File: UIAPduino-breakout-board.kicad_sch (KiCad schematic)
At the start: 13 parts, among them J1 Conn_01x20_Pin, J2 Conn_01x20_Socket, J3 Barrel_Jack_Switch, U3 L7805

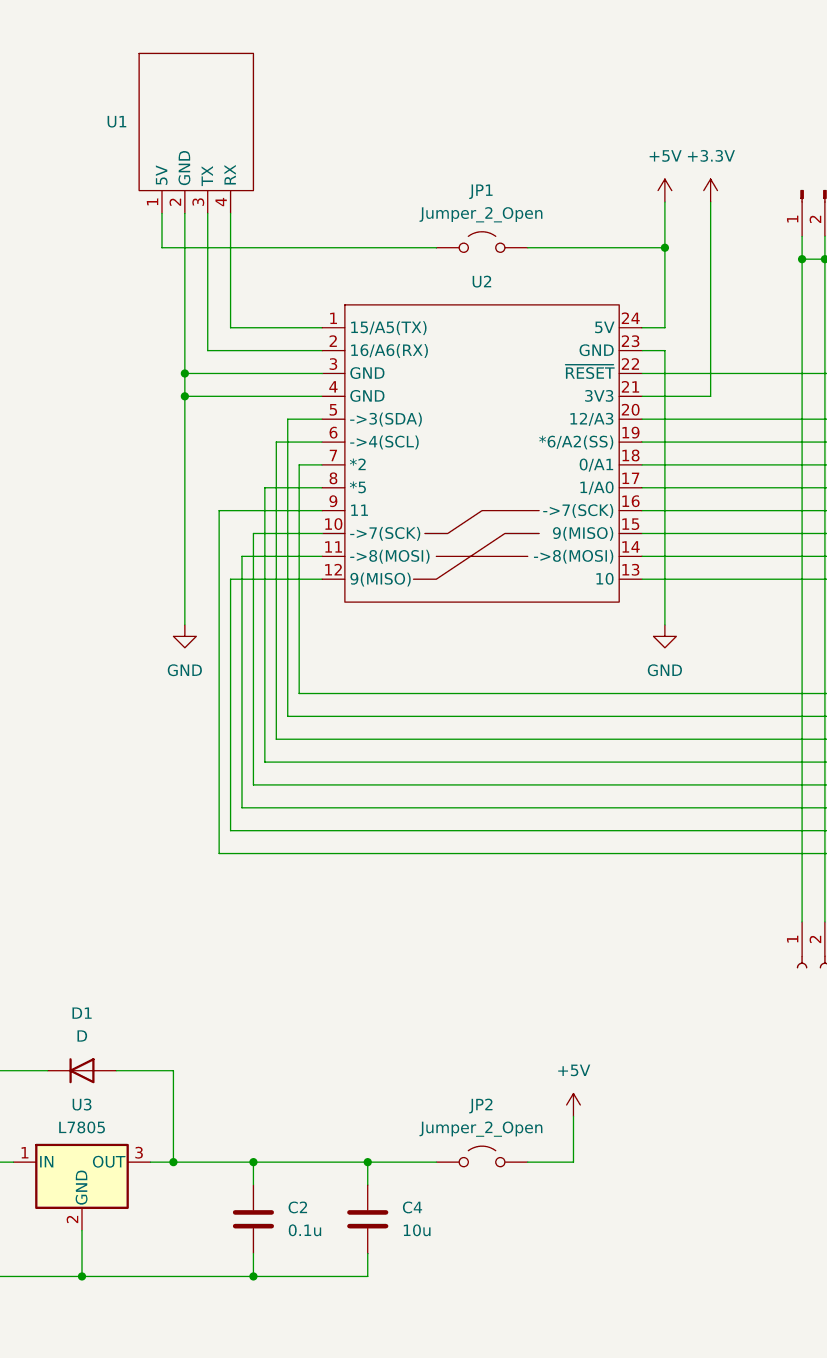
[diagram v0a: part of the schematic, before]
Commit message: ジャンパをスイッチに変更
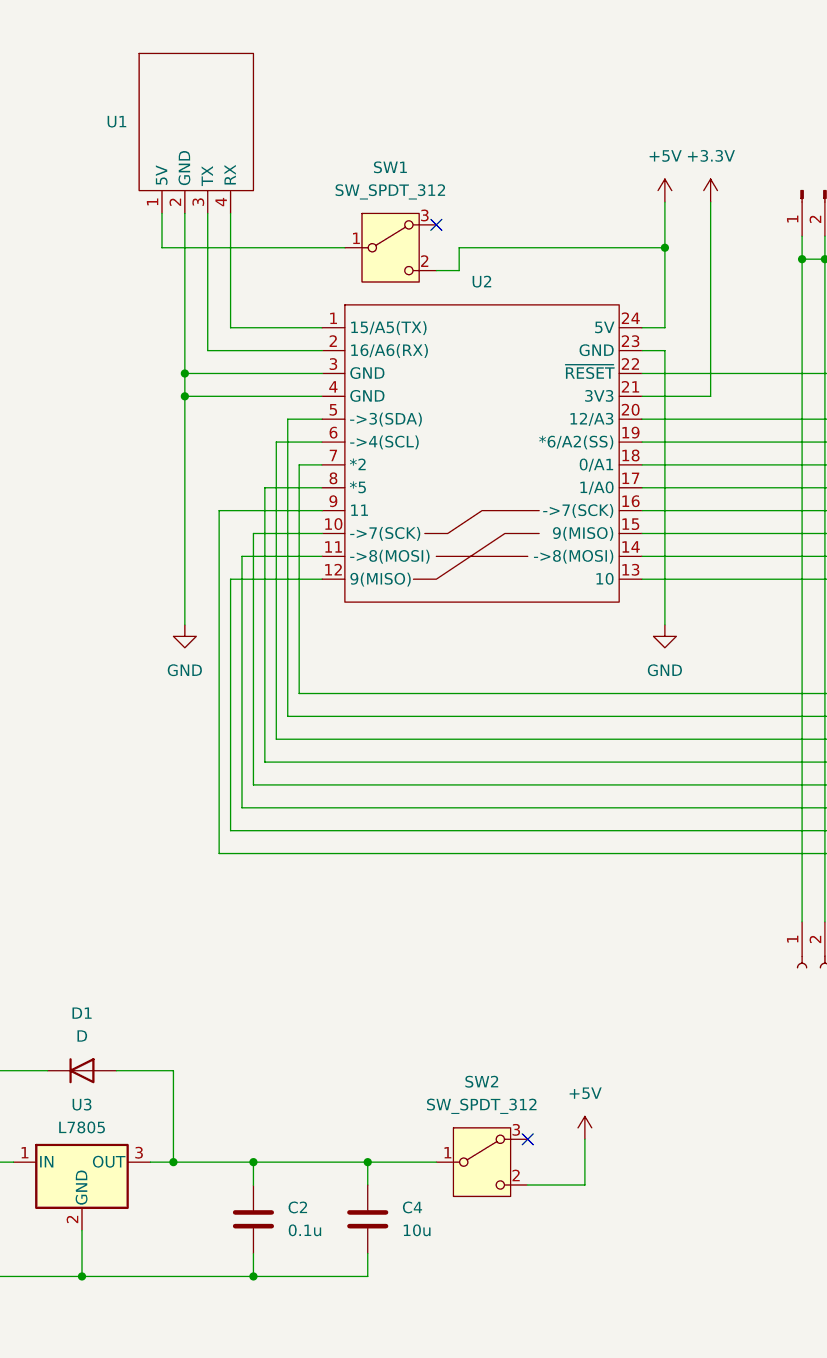
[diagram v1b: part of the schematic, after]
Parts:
- removed JP1, JP2: Jumper_2_Open, Jumper:SolderJumper-2_P1.3mm_Open_TrianglePad1.0x1.5mm, symbol Jumper:Jumper_2_Open
- added SW1, SW2: SW_SPDT_312, Button_Switch_THT:SW_Slide-03_Wuerth-WS-SLTV_10x2.5x6.4_P2.54mm, symbol Switch:SW_SPDT_312
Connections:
- net +5V: now also SW1.2 (C), SW2.2 (C)
- net at U1.1 (5V): now also SW1.1 (B)
- net at C2.1, C4.1, D1.2 (A)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: now also SW2.1 (B)
- no-connect marks 0 -> 2

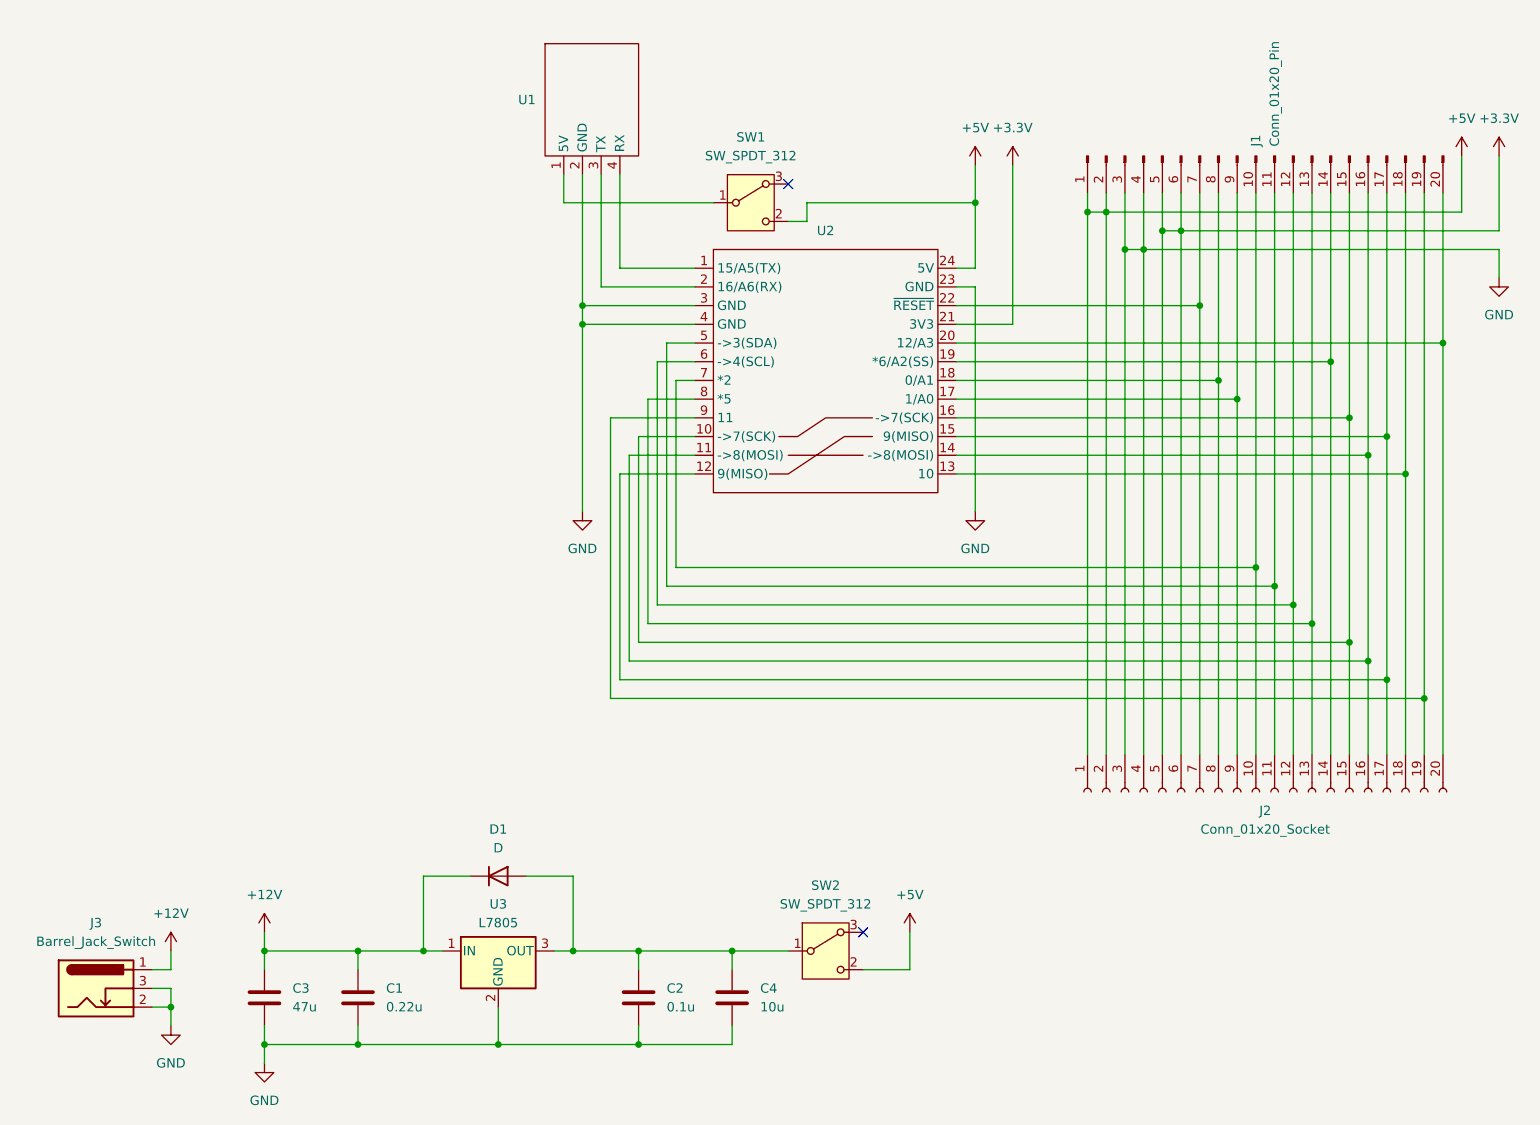
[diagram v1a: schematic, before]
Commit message: UART 接続先切り替え用スイッチを追加
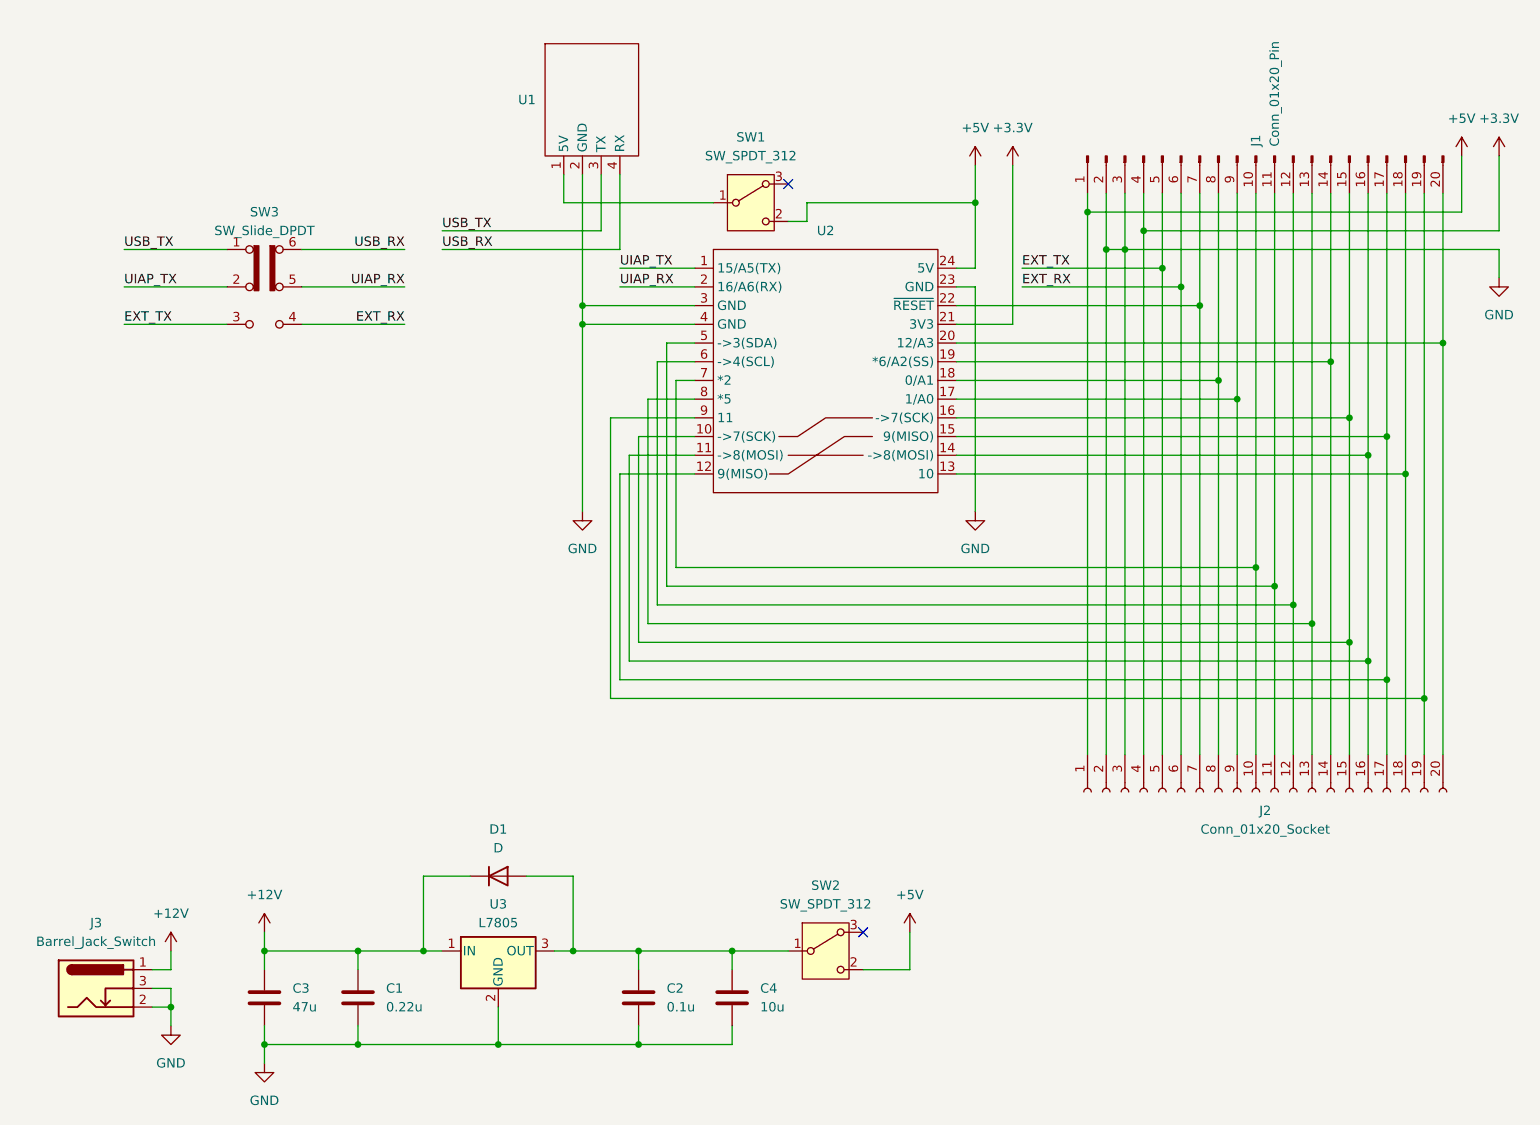
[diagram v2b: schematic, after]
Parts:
- added SW3: SW_Slide_DPDT, Button_Switch_THT:SW_CK_JS202011CQN_DPDT_Straight, symbol Switch:SW_Slide_DPDT
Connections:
- net +3.3V: now also J1.4 (Pin_4), J2.4 (Pin_4); no longer J1.5 (Pin_5), J1.6 (Pin_6), J2.5 (Pin_5), J2.6 (Pin_6)
- net +5V: no longer J1.2 (Pin_2), J2.2 (Pin_2)
- net GND: now also J1.2 (Pin_2), J2.2 (Pin_2); no longer J1.4 (Pin_4), J2.4 (Pin_4)
- net UIAP_RX: now reaches U2.2 (16/A6(RX))
- net UIAP_RX: now also SW3.5 (B); no longer U1.3 (TX)
- net UIAP_TX: now reaches U2.1 (15/A5(TX))
- net UIAP_TX: now also SW3.2 (B); no longer U1.4 (RX)
- new net EXT_RX: J1.6 (Pin_6), J2.6 (Pin_6), SW3.4 (A)
- new net EXT_TX: J1.5 (Pin_5), J2.5 (Pin_5), SW3.3 (C)
- new net USB_RX: SW3.6 (C), U1.4 (RX)
- new net USB_TX: SW3.1 (A), U1.3 (TX)

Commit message: 配線修正
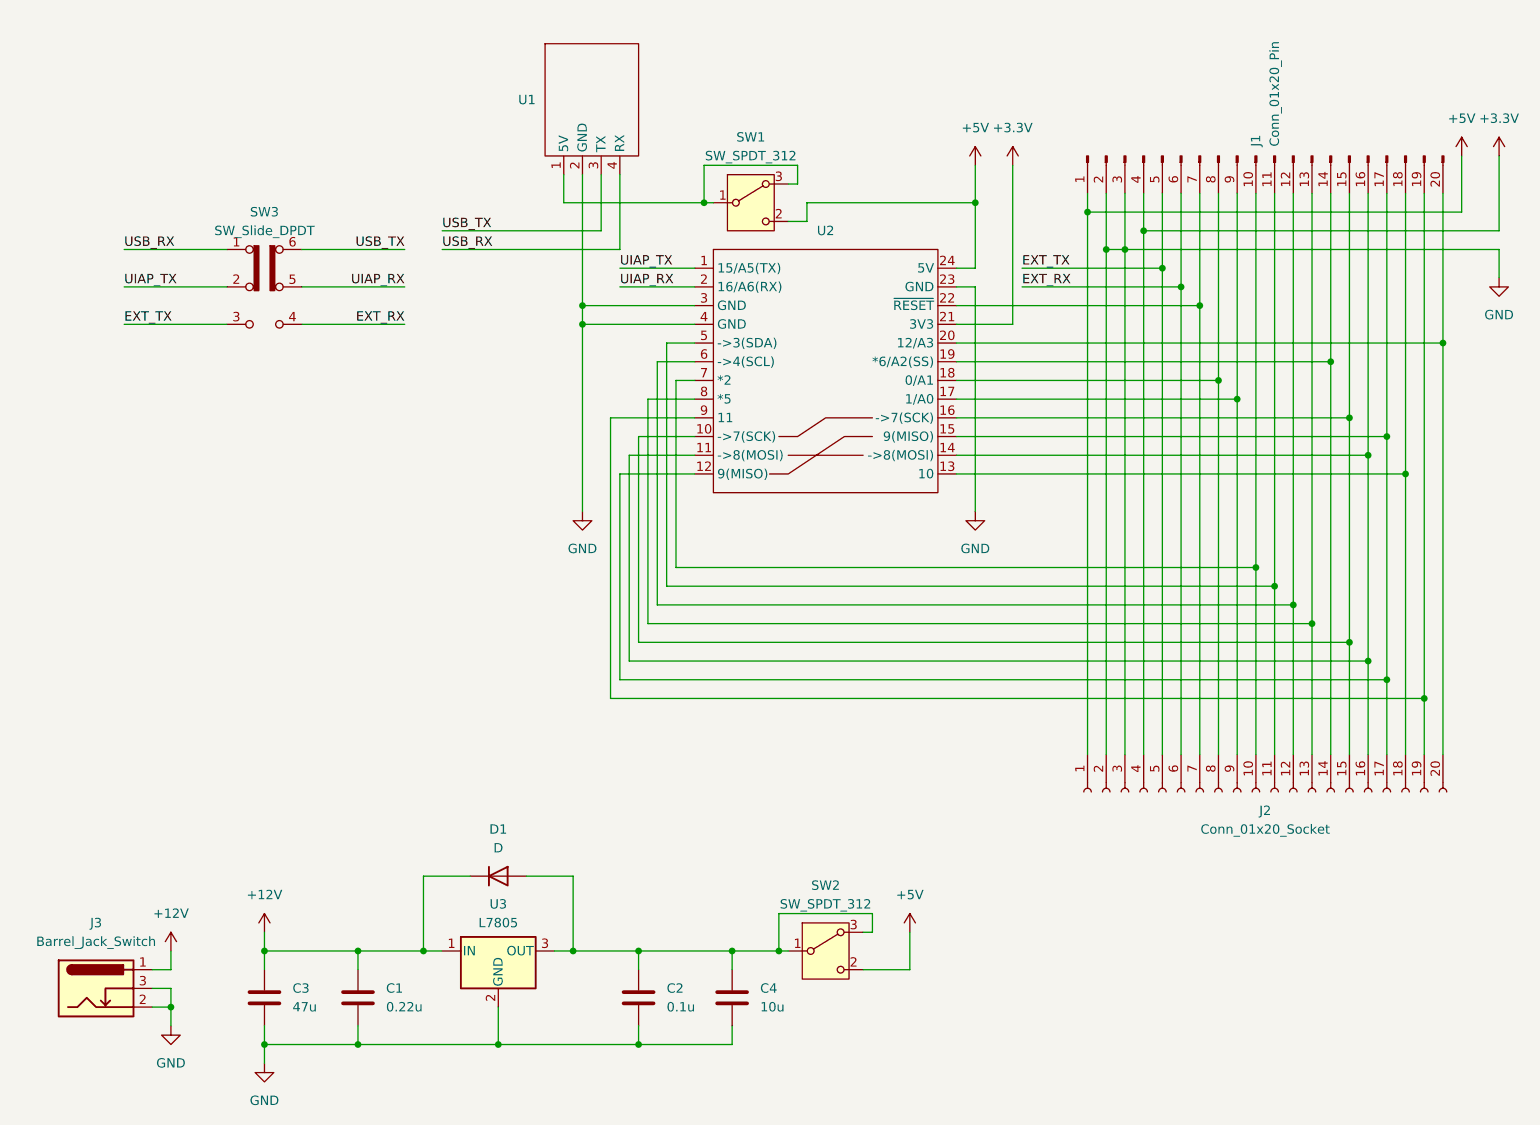
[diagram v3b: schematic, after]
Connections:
- net USB_RX: now also SW3.1 (A); no longer SW3.6 (C)
- net USB_TX: now also SW3.6 (C); no longer SW3.1 (A)
- net at C2.1, C4.1, D1.2 (A)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: now also SW2.3 (A)
- net at SW1.1 (B), U1.1 (5V): now also SW1.3 (A)
- no-connect marks 2 -> 0
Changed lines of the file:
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@@
+	)
+	(junction
+		(at 146.05 153.67)
+		(diameter 0)
+		(color 0 0 0 0)
 	)
 	(junction
@@
 		(color 0 0 0 0)
 	)
-	(no_connect
-		(at 147.32 49.53)
-	)
-	(no_connect
-		(at 157.48 151.13)
+	(junction
+		(at 135.89 52.07)
+		(diameter 0)
+		(color 0 0 0 0)
 	)
 	(wire
@@
 	(wire
 		(pts
+			(xy 158.75 148.59) (xy 146.05 148.59)
+		)
+		(stroke
+			(width 0)
+			(type default)
+		)
+	)
+	(wire
+		(pts
 			(xy 127 166.37) (xy 127 163.83)
 		)
@@
 	(wire
 		(pts
-			(xy 147.32 153.67) (xy 139.7 153.67)
+			(xy 147.32 153.67) (xy 146.05 153.67)
 		)
 		(stroke
@@
 	(wire
 		(pts
+			(xy 148.59 49.53) (xy 147.32 49.53)
+		)
+		(stroke
+			(width 0)
+			(type default)
+		)
+	)
+	(wire
+		(pts
 			(xy 132.08 76.2) (xy 134.62 76.2)
 		)
@@
 	(wire
 		(pts
-			(xy 116.84 52.07) (xy 137.16 52.07)
+			(xy 116.84 52.07) (xy 135.89 52.07)
 		)
 		(stroke
@@
 	(wire
 		(pts
+			(xy 135.89 52.07) (xy 135.89 46.99)
+		)
+		(stroke
+			(width 0)
+			(type default)
+		)
+	)
+	(wire
+		(pts
 			(xy 127 83.82) (xy 127 111.76)
 		)
@@
 	(wire
 		(pts
+			(xy 146.05 153.67) (xy 139.7 153.67)
+		)
+		(stroke
+			(width 0)
+			(type default)
+		)
+	)
+	(wire
+		(pts
 			(xy 231.14 88.9) (xy 231.14 50.8)
 		)
@@
 	(wire
 		(pts
+			(xy 148.59 46.99) (xy 148.59 49.53)
+		)
+		(stroke
+			(width 0)
+			(type default)
+		)
+	)
+	(wire
+		(pts
 			(xy 134.62 83.82) (xy 127 83.82)
 		)
@@
 	(wire
 		(pts
+			(xy 135.89 52.07) (xy 137.16 52.07)
+		)
+		(stroke
+			(width 0)
+			(type default)
+		)
+	)
+	(wire
+		(pts
 			(xy 129.54 73.66) (xy 129.54 106.68)
 		)
@@
 	(wire
 		(pts
+			(xy 135.89 46.99) (xy 148.59 46.99)
+		)
+		(stroke
+			(width 0)
+			(type default)
+		)
+	)
+	(wire
+		(pts
 			(xy 238.76 45.72) (xy 238.76 53.34)
 		)
@@
 	(wire
 		(pts
+			(xy 157.48 151.13) (xy 158.75 151.13)
+		)
+		(stroke
+			(width 0)
+			(type default)
+		)
+	)
+	(wire
+		(pts
 			(xy 124.46 63.5) (xy 134.62 63.5)
 		)
@@
 	(wire
 		(pts
+			(xy 158.75 151.13) (xy 158.75 148.59)
+		)
+		(stroke
+			(width 0)
+			(type default)
+		)
+	)
+	(wire
+		(pts
 			(xy 231.14 127) (xy 231.14 88.9)
 		)
@@
 		(pts
 			(xy 104.14 143.51) (xy 97.79 143.51)
+		)
+		(stroke
+			(width 0)
+			(type default)
+		)
+	)
+	(wire
+		(pts
+			(xy 146.05 148.59) (xy 146.05 153.67)
 		)
 		(stroke
@@
 		)
 	)
-	(label "USB_TX"
+	(label "USB_RX"
 		(at 57.15 58.42 0)
 		(fields_autoplaced yes)
@@
 		)
 	)
-	(label "USB_RX"
+	(label "USB_TX"
 		(at 95.25 58.42 180)
 		(fields_autoplaced yes)
